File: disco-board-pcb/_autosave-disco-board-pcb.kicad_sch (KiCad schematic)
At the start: 140 parts, among them J1 Conn_02x32_Odd_Even, J2 Conn_02x32_Odd_Even, U1 MMA8653FCR1

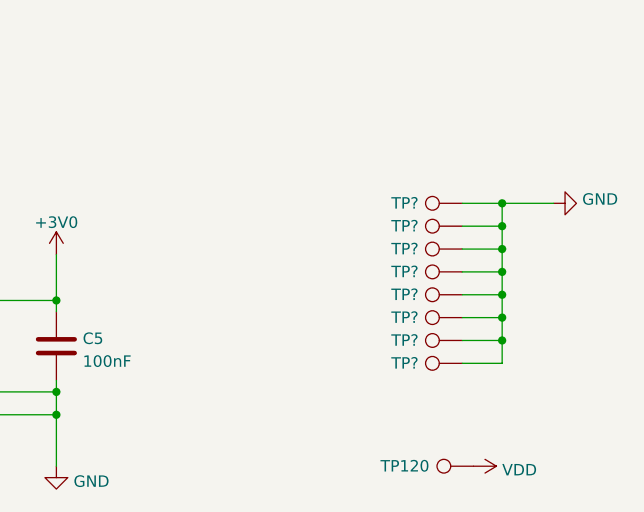
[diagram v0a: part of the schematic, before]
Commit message: Routed all test points
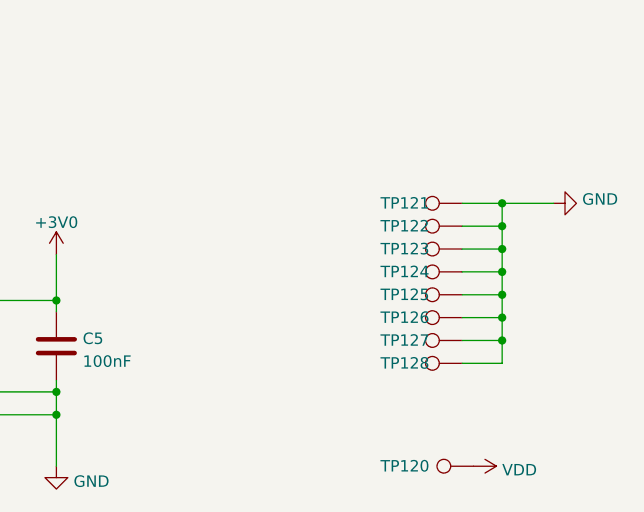
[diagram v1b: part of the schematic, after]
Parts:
- gave numbers to parts that had none: 8
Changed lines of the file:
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@@
   (symbol (lib_id "Connector:TestPoint") (at 156.845 221.615 90) (unit 1)
     (in_bom yes) (on_board yes)
-    (property "Reference" "TP?" (id 0) (at 150.495 221.615 90))
+    (property "Reference" "TP128" (id 0) (at 150.495 221.615 90))
     (property "Value" "TestPoint" (id 1) (at 152.146 219.9128 90)
       (effects (font (size 1.27 1.27)) (justify left) hide)
@@
   (symbol (lib_id "Connector:TestPoint") (at 156.845 213.995 90) (unit 1)
     (in_bom yes) (on_board yes)
-    (property "Reference" "TP?" (id 0) (at 150.495 213.995 90))
+    (property "Reference" "TP125" (id 0) (at 150.495 213.995 90))
     (property "Value" "TestPoint" (id 1) (at 152.146 212.2928 90)
       (effects (font (size 1.27 1.27)) (justify left) hide)
@@
   (symbol (lib_id "Connector:TestPoint") (at 156.845 219.075 90) (unit 1)
     (in_bom yes) (on_board yes)
-    (property "Reference" "TP?" (id 0) (at 150.495 219.075 90))
+    (property "Reference" "TP127" (id 0) (at 150.495 219.075 90))
     (property "Value" "TestPoint" (id 1) (at 152.146 217.3728 90)
       (effects (font (size 1.27 1.27)) (justify left) hide)
@@
   (symbol (lib_id "Connector:TestPoint") (at 156.845 216.535 90) (unit 1)
     (in_bom yes) (on_board yes)
-    (property "Reference" "TP?" (id 0) (at 150.495 216.535 90))
+    (property "Reference" "TP126" (id 0) (at 150.495 216.535 90))
     (property "Value" "TestPoint" (id 1) (at 152.146 214.8328 90)
       (effects (font (size 1.27 1.27)) (justify left) hide)
@@
   (symbol (lib_id "Connector:TestPoint") (at 156.845 208.915 90) (unit 1)
     (in_bom yes) (on_board yes)
-    (property "Reference" "TP?" (id 0) (at 150.495 208.915 90))
+    (property "Reference" "TP123" (id 0) (at 150.495 208.915 90))
     (property "Value" "TestPoint" (id 1) (at 152.146 207.2128 90)
       (effects (font (size 1.27 1.27)) (justify left) hide)
@@
   (symbol (lib_id "Connector:TestPoint") (at 156.845 203.835 90) (unit 1)
     (in_bom yes) (on_board yes)
-    (property "Reference" "TP?" (id 0) (at 150.495 203.835 90))
+    (property "Reference" "TP121" (id 0) (at 150.495 203.835 90))
     (property "Value" "TestPoint" (id 1) (at 152.146 202.1328 90)
       (effects (font (size 1.27 1.27)) (justify left) hide)
@@
   (symbol (lib_id "power:GND") (at 167.005 203.835 90) (unit 1)
     (in_bom yes) (on_board yes) (fields_autoplaced)
-    (property "Reference" "#PWR?" (id 0) (at 173.355 203.835 0)
+    (property "Reference" "#PWR0101" (id 0) (at 173.355 203.835 0)
       (effects (font (size 1.27 1.27)) hide)
     )
@@
   (symbol (lib_id "Connector:TestPoint") (at 156.845 206.375 90) (unit 1)
     (in_bom yes) (on_board yes)
-    (property "Reference" "TP?" (id 0) (at 150.495 206.375 90))
+    (property "Reference" "TP122" (id 0) (at 150.495 206.375 90))
     (property "Value" "TestPoint" (id 1) (at 152.146 204.6728 90)
       (effects (font (size 1.27 1.27)) (justify left) hide)
@@
   (symbol (lib_id "Connector:TestPoint") (at 156.845 211.455 90) (unit 1)
     (in_bom yes) (on_board yes)
-    (property "Reference" "TP?" (id 0) (at 150.495 211.455 90))
+    (property "Reference" "TP124" (id 0) (at 150.495 211.455 90))
     (property "Value" "TestPoint" (id 1) (at 152.146 209.7528 90)
       (effects (font (size 1.27 1.27)) (justify left) hide)
@@
     )
     (path "/cb06ceba-6243-4549-bef1-903e90205322"
-      (reference "#PWR?") (unit 1) (value "GND") (footprint "")
+      (reference "#PWR0101") (unit 1) (value "GND") (footprint "")
     )
     (path "/927ac2c7-5f63-4d17-b9d2-5c71e37a548d"
@@
       (reference "TP120") (unit 1) (value "TestPoint") (footprint "TestPoint:TestPoint_Pad_D1.5mm")
     )
+    (path "/a3dd6d5e-24ce-451d-b4aa-01d4c0ff1c0b"
+      (reference "TP121") (unit 1) (value "TestPoint") (footprint "TestPoint:TestPoint_Pad_D1.5mm")
+    )
+    (path "/d3427dd9-00a1-4b49-9fef-2523776bf9cb"
+      (reference "TP122") (unit 1) (value "TestPoint") (footprint "TestPoint:TestPoint_Pad_D1.5mm")
+    )
+    (path "/a00d6244-4004-4654-b8bb-f9138d30bb56"
+      (reference "TP123") (unit 1) (value "TestPoint") (footprint "TestPoint:TestPoint_Pad_D1.5mm")
+    )
+    (path "/ddc5318c-a26c-4437-b803-d3049f0a9b09"
+      (reference "TP124") (unit 1) (value "TestPoint") (footprint "TestPoint:TestPoint_Pad_D1.5mm")
+    )
+    (path "/36e462b6-15d1-4683-9eda-a167600c74c2"
+      (reference "TP125") (unit 1) (value "TestPoint") (footprint "TestPoint:TestPoint_Pad_D1.5mm")
+    )
+    (path "/9bd6212a-3993-4904-9135-d74eb822c60a"
+      (reference "TP126") (unit 1) (value "TestPoint") (footprint "TestPoint:TestPoint_Pad_D1.5mm")
+    )
+    (path "/3da7d40b-050e-43da-adfb-bdf4ded032dd"
+      (reference "TP127") (unit 1) (value "TestPoint") (footprint "TestPoint:TestPoint_Pad_D1.5mm")
+    )
     (path "/04620c9b-faea-4c13-baaf-7f7ece0a96e1"
-      (reference "TP?") (unit 1) (value "TestPoint") (footprint "TestPoint:TestPoint_Pad_D1.5mm")
-    )
-    (path "/36e462b6-15d1-4683-9eda-a167600c74c2"
-      (reference "TP?") (unit 1) (value "TestPoint") (footprint "TestPoint:TestPoint_Pad_D1.5mm")
-    )
-    (path "/3da7d40b-050e-43da-adfb-bdf4ded032dd"
-      (reference "TP?") (unit 1) (value "TestPoint") (footprint "TestPoint:TestPoint_Pad_D1.5mm")
-    )
-    (path "/9bd6212a-3993-4904-9135-d74eb822c60a"
-      (reference "TP?") (unit 1) (value "TestPoint") (footprint "TestPoint:TestPoint_Pad_D1.5mm")
-    )
-    (path "/a00d6244-4004-4654-b8bb-f9138d30bb56"
-      (reference "TP?") (unit 1) (value "TestPoint") (footprint "TestPoint:TestPoint_Pad_D1.5mm")
-    )
-    (path "/a3dd6d5e-24ce-451d-b4aa-01d4c0ff1c0b"
-      (reference "TP?") (unit 1) (value "TestPoint") (footprint "TestPoint:TestPoint_Pad_D1.5mm")
-    )
-    (path "/d3427dd9-00a1-4b49-9fef-2523776bf9cb"
-      (reference "TP?") (unit 1) (value "TestPoint") (footprint "TestPoint:TestPoint_Pad_D1.5mm")
-    )
-    (path "/ddc5318c-a26c-4437-b803-d3049f0a9b09"
-      (reference "TP?") (unit 1) (value "TestPoint") (footprint "TestPoint:TestPoint_Pad_D1.5mm")
+      (reference "TP128") (unit 1) (value "TestPoint") (footprint "TestPoint:TestPoint_Pad_D1.5mm")
     )
     (path "/c2c1c04a-fec3-4a00-a18d-b12320c134e4"
